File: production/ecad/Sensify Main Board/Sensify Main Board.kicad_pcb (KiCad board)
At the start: 4 copper layers, 143 parts, among them J1 1-2834011-3, J2 1-2834011-2, J3 1332645, J4 0532611271, J6 Conn_01x02_Socket, J7 Conn_01x02_Socket, J8 Conn_01x02_Socket, J9 Conn_01x02_Socket, Q1 2N700, Q2 PMPB13XNE,115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

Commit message: put in TPs + haptics half placed + tried to fit stuff in more
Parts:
- removed BAT2-_TP1: TestPoint, TestPoint:TestPoint_Pad_D1.5mm
- moved TP2 118.3 mm to (148.6, 166.6), turned to 90 degrees
- moved TP3 109.2 mm to (154.9, 164.2)
- moved TP5 95.3 mm to (144.3, 126.6)
- moved TP4 72.4 mm to (163.1, 99.1)
- moved USB_9V+1 57.8 mm to (157.7, 167.3)
- moved J9 57.2 mm to (156.2, 117.9)
- moved U9 51.9 mm to (155.7, 107.8), turned to -90 degrees
- moved C36 50.1 mm to (158.1, 109.7), turned to 90 degrees
- moved C34 47.7 mm to (158.1, 105.9), turned to -90 degrees
- moved TP1 47.5 mm to (188.1, 77.2)
- moved TP6 47.5 mm to (189.1, 66.5)
- moved TP7 47.5 mm to (185.0, 68.4)
- moved TP8 47.5 mm to (183.8, 64.1)
- moved TH1_TP1 45.5 mm to (143.8, 148.5)
- moved J8 39.6 mm to (156.3, 134.3)
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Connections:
- SW1 pad 1: IO0 -> GND
- SW1 pad 2: GND -> IO0
- SW2 pad 1: EN -> GND
- SW2 pad 2: GND -> EN
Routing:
- net SCL: track 2.27 -> 21.9 mm
- net HAPTICS_EN: track 0.00 -> 19.1 mm
- net SDA: track 3.42 -> 21.2 mm
- net GND: track 46.6 -> 63.6 mm, vias 20 -> 23
- net +5V: track 37.3 -> 27.4 mm
- net RTS: track 13.6 -> 4.39 mm
- net /Haptics/LRA_OUT3+: track 0.00 -> 9.01 mm
- net /Haptics/LRA_OUT4+: track 0.00 -> 8.70 mm
- net IO0: track 4.48 -> 11.2 mm
- net BMS_ALERT: track 26.8 -> 20.9 mm
- net /Haptics/LRA_OUT3-: track 0.00 -> 5.80 mm
- net /Haptics/LRA_OUT4-: track 0.00 -> 5.79 mm
- net Net-(U4-VIN): track 36.6 -> 31.4 mm
- net Net-(Q5-Pad1): track 4.93 -> 1.91 mm
- net Net-(Q6-Pad1): track 6.29 -> 9.29 mm
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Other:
- board text added: "C35 ref deg idk"
- board text added: "maybe move U9 away from edge to make space for haptic connector"

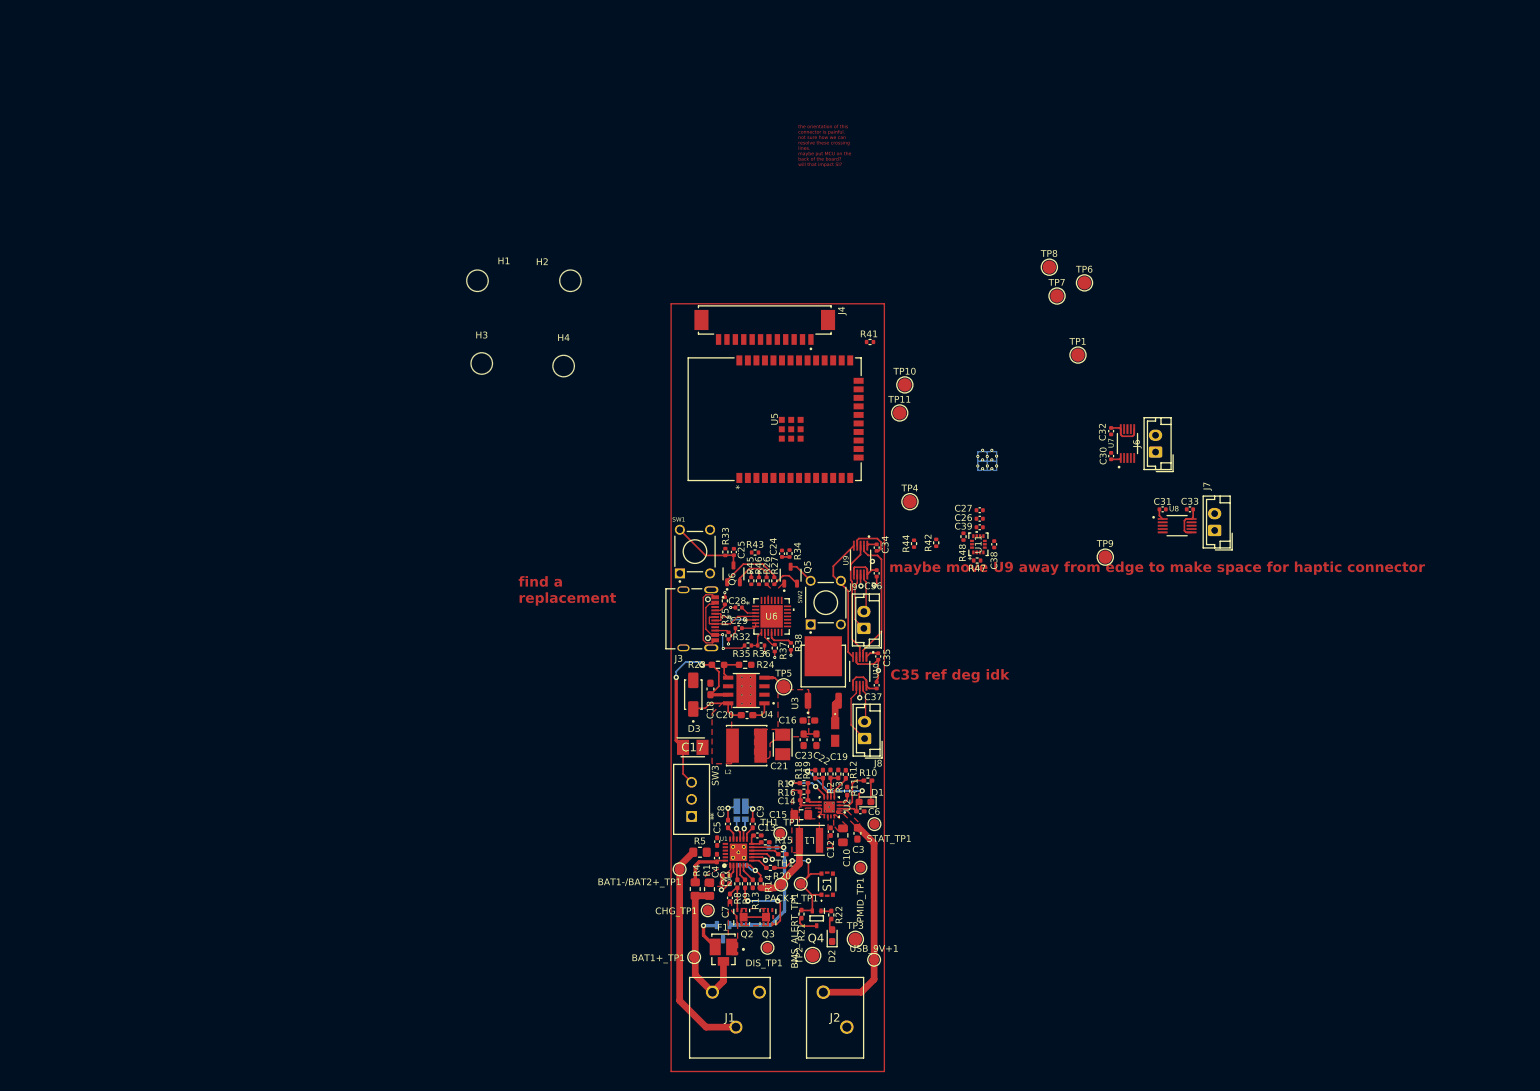
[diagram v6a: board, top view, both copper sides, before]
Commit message: Finished UART, Haptics, and IMU
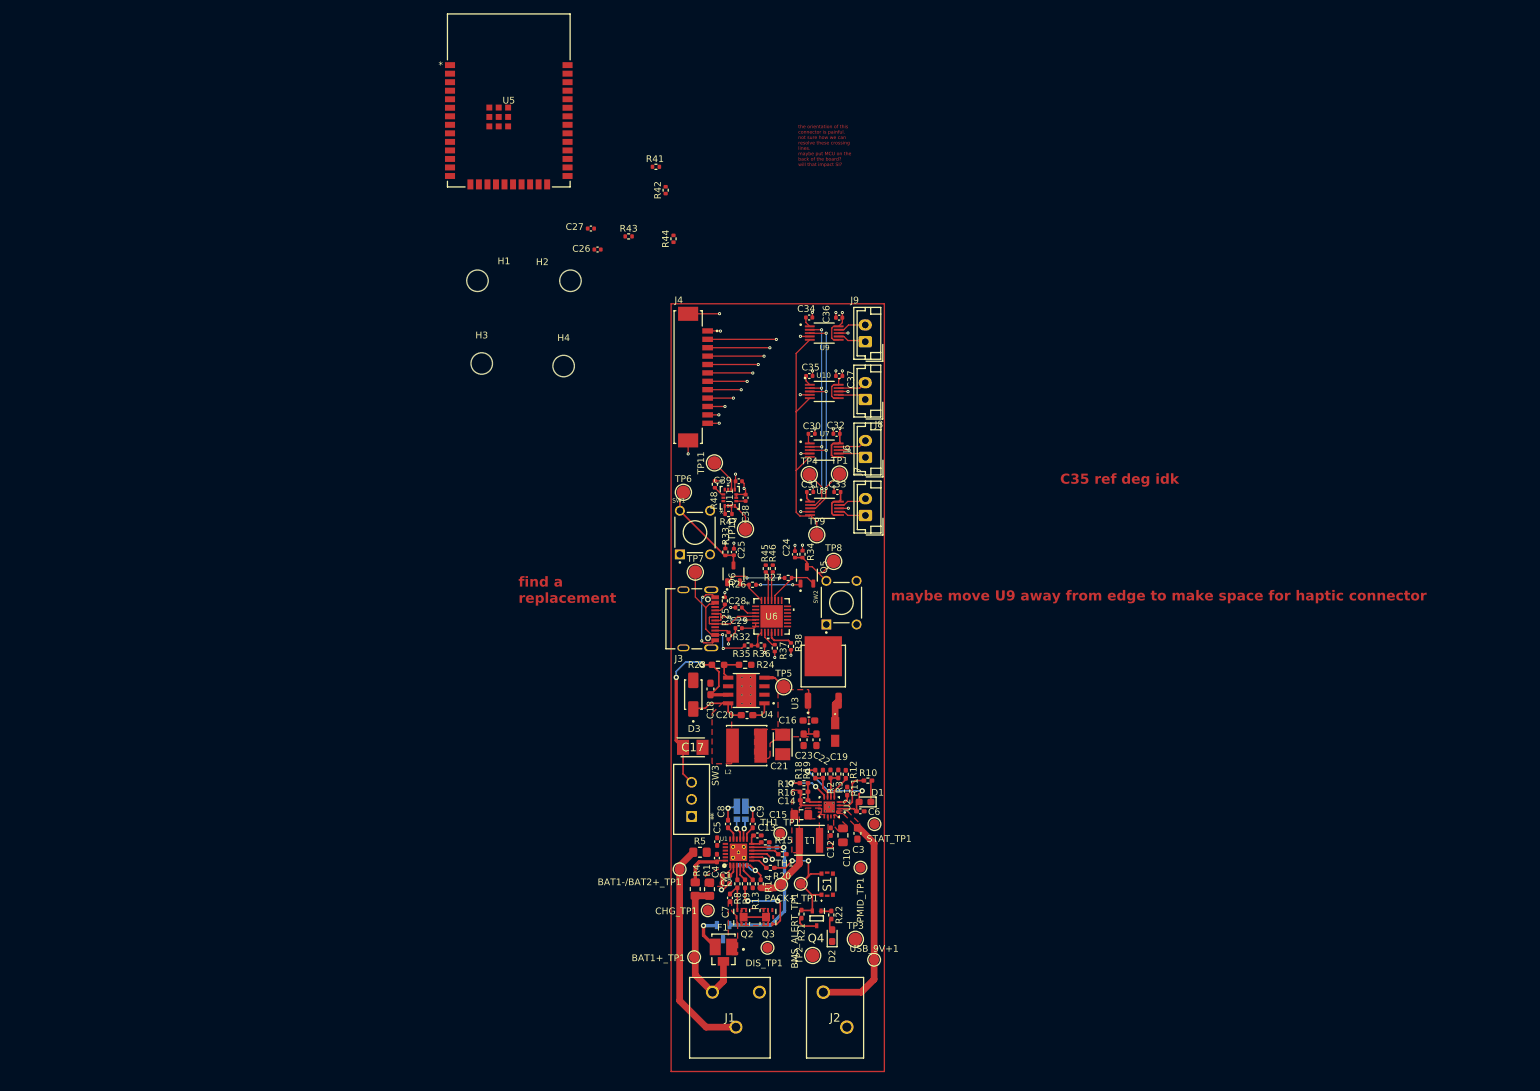
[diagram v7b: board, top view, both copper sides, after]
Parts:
- moved C27 71.5 mm to (115.6, 58.4)
- moved C26 69.6 mm to (116.6, 61.5)
- moved TP7 67.8 mm to (131.1, 109.6)
- moved TP6 67.4 mm to (129.3, 97.7)
- moved R42 66.2 mm to (126.7, 52.7)
- moved U5 61.8 mm to (103.3, 39.3), turned to 0 degrees
- moved R44 57.8 mm to (127.9, 59.9)
- moved TP8 54.3 mm to (151.7, 108.0)
- moved C33 52.6 mm to (152.3, 97.6)
- moved U8 52.6 mm to (150.4, 100.1)
- moved C31 52.6 mm to (148.2, 97.6)
- moved J7 52.0 mm to (156.4, 101.1)
- moved R43 50.7 mm to (121.2, 59.6)
- moved J8 50.5 mm to (156.4, 83.8)
- moved C37 46.4 mm to (152.5, 80.4), turned to 0 degrees
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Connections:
- J4 pad 10: GND -> NovelMechPin10
- U5 pad 9: unconnected-(U5-IO33-Pad9) -> NovelMechPin10
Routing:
- net SDA: track 21.2 -> 41.9 mm, vias 1 -> 5
- net HAPTICS_EN: track 19.1 -> 38.0 mm
- net SCL: track 21.9 -> 37.7 mm, vias 1 -> 5
- net NovelMechPin2: track 0.00 -> 10.2 mm, vias 0 -> 1
- net +3V3: track 11.1 -> 21.0 mm, vias 2 -> 7
- net NovelMechPin3: track 0.00 -> 9.28 mm, vias 0 -> 1
- net NovelMechPin4: track 0.00 -> 8.41 mm, vias 0 -> 1
- net GND: track 63.6 -> 55.9 mm, vias 23 -> 30
- net NovelMechPin5: track 0.00 -> 7.54 mm, vias 0 -> 1
- net NovelMechPin6: track 0.00 -> 6.74 mm, vias 0 -> 1
- net FLASHING_VBUS_5V: track 13.4 -> 19.3 mm
- net NovelMechPin7: track 0.00 -> 5.90 mm, vias 0 -> 1
- net INTERRUPT2_IMU: track 0.00 -> 5.03 mm
- net NovelMechPin8: track 0.00 -> 5.01 mm, vias 0 -> 1
- net Net-(Q5-Pad1): track 1.91 -> 6.71 mm, vias 0 -> 2
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
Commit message: changed tp names + attempted to start placing mcu and making space for mounting holes?
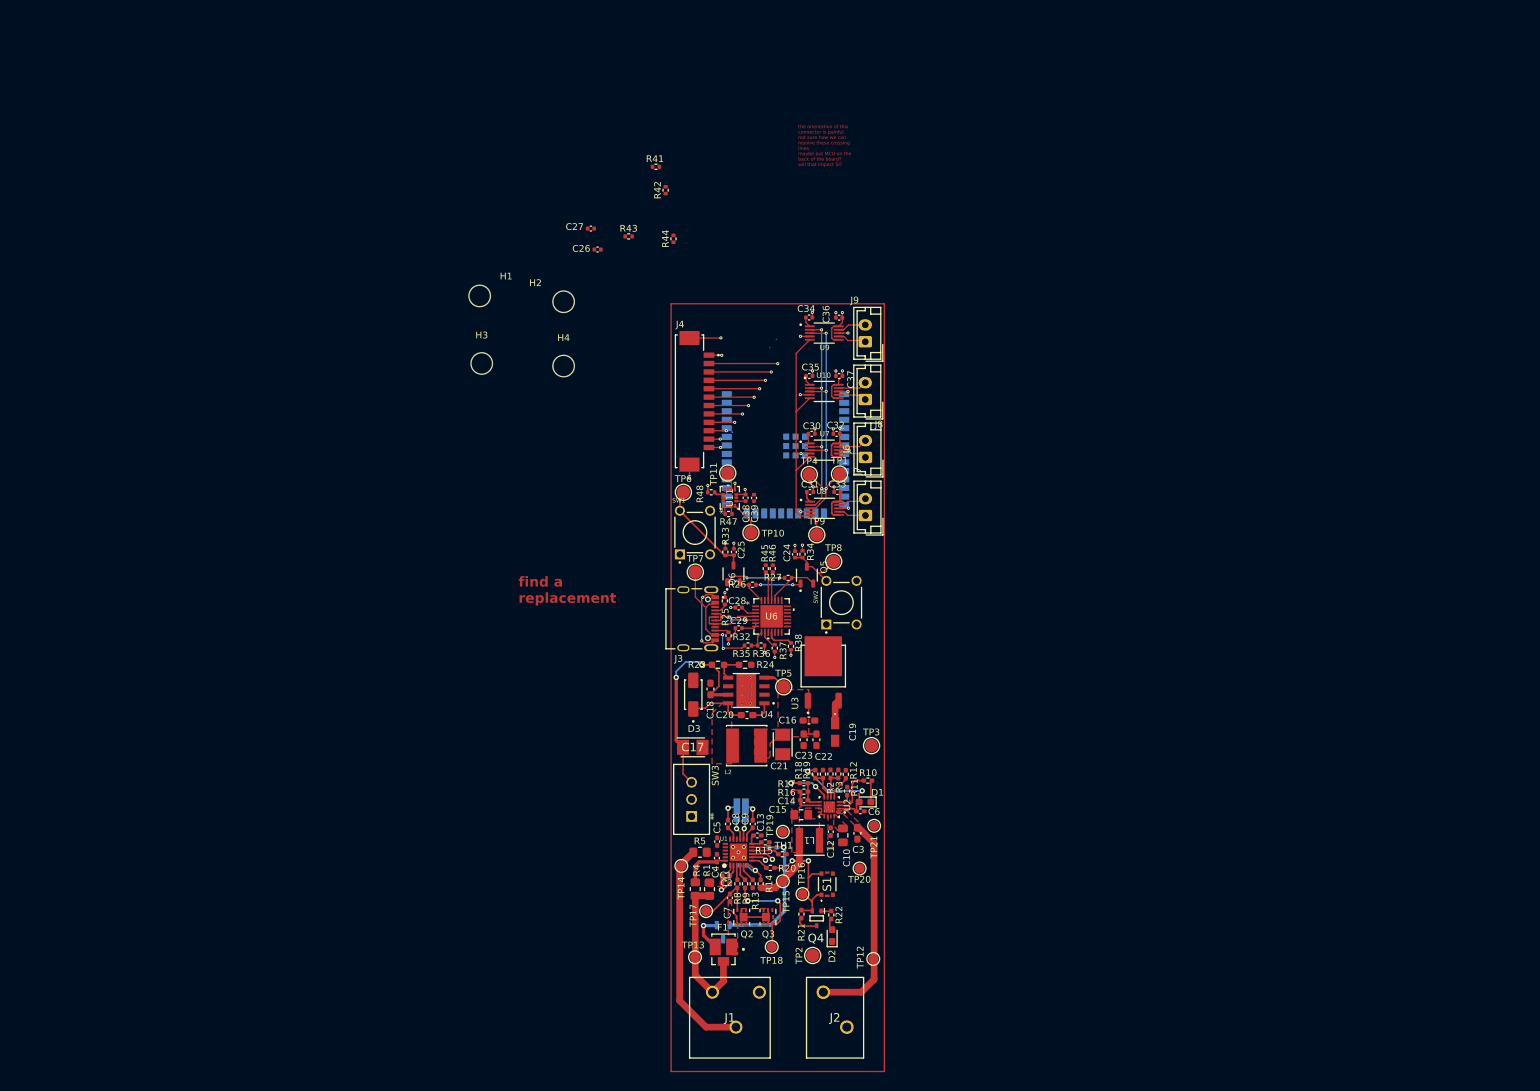
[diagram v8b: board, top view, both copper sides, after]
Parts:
- removed BAT1+_TP1, BAT1-/BAT2+_TP1, BMS_ALERT_TP1, CHG_TP1, DIS_TP1, PACK+_TP1, PMID_TP1, STAT_TP1, TH1_TP1, USB_9V+1: TestPoint, TestPoint:TestPoint_Pad_D1.5mm
- added TP12: TestPoint, TestPoint:TestPoint_Pad_D1.5mm, F.Cu at (157.6, 167.1)
- added TP13: TestPoint, TestPoint:TestPoint_Pad_D1.5mm, F.Cu at (131.1, 166.9)
- added TP14: TestPoint, TestPoint:TestPoint_Pad_D1.5mm, F.Cu at (129.0, 153.3)
- added TP15: TestPoint, TestPoint:TestPoint_Pad_D1.5mm, F.Cu at (144.1, 155.6)
- added TP16: TestPoint, TestPoint:TestPoint_Pad_D1.5mm, F.Cu at (147.1, 157.5)
- added TP17: TestPoint, TestPoint:TestPoint_Pad_D1.5mm, F.Cu at (132.7, 160.0)
- added TP18: TestPoint, TestPoint:TestPoint_Pad_D1.5mm, F.Cu at (142.5, 165.4)
- added TP19: TestPoint, TestPoint:TestPoint_Pad_D1.5mm, F.Cu at (144.1, 148.2)
- added TP20: TestPoint, TestPoint:TestPoint_Pad_D1.5mm, F.Cu at (155.6, 153.7)
- added TP21: TestPoint, TestPoint:TestPoint_Pad_D1.5mm, F.Cu at (157.7, 147.3)
- U5: moved to B.Cu
- moved U5 64.0 mm to (144.5, 88.3), turned to 180 degrees
- moved TP3 28.9 mm to (157.4, 135.4)
- moved J4 3.61 mm to (130.2, 84.1)
- moved C39 3.36 mm to (139.9, 98.5), turned to 90 degrees
- moved H2 3.29 mm to (111.5, 69.3)
- moved TP11 2.49 mm to (135.9, 94.8)
- moved H1 2.28 mm to (99.0, 68.4)
- moved R48 1.31 mm to (133.5, 97.7), turned to 180 degrees
- moved TP10 0.97 mm to (139.4, 103.7)
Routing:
- net Net-(Q2-G): track 4.85 -> 9.45 mm
- net Net-(Q3-G): track 11.1 -> 15.1 mm
- net INTERRUPT2_IMU: track 5.03 -> 2.70 mm
- net GND: track 55.9 -> 54.5 mm
- net +3V3: track 21.0 -> 19.9 mm
- net INTERRUPT1_IMU: track 4.30 -> 5.21 mm
- net BMS_ALERT: track 20.9 -> 20.0 mm
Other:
- board text removed: "C35 ref deg idk"
- board text removed: "maybe move U9 away from edge to make space for haptic connector"
